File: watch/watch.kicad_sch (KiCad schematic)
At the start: 126 parts, among them IC1 MAX77659AENV+, IC2 MAX86141ENP+T, IC3 MAX32664GTGC+T, IC4 TXS0108ERGYR, IC6 MAX31341CETB+T, J1 TYPE-C-31-M-12, J2 Conn_01x01_Pin, J3 Conn_ARM_JTAG_SWD_10, J4 505110-2291, J5 Conn_01x01_Pin, J6 Conn_01x01_Pin, J7 Conn_01x01_Pin, Q1 BSS138, U1 nRF52840, U2 ICM-20602, Y1 FA-128_32.0000MF10Z-AJ5, Y2 CM7V-T1A-32.768kHz-6pF-20PPM-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, Y3 CM7V-T1A-32.768kHz-6pF-20PPM-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

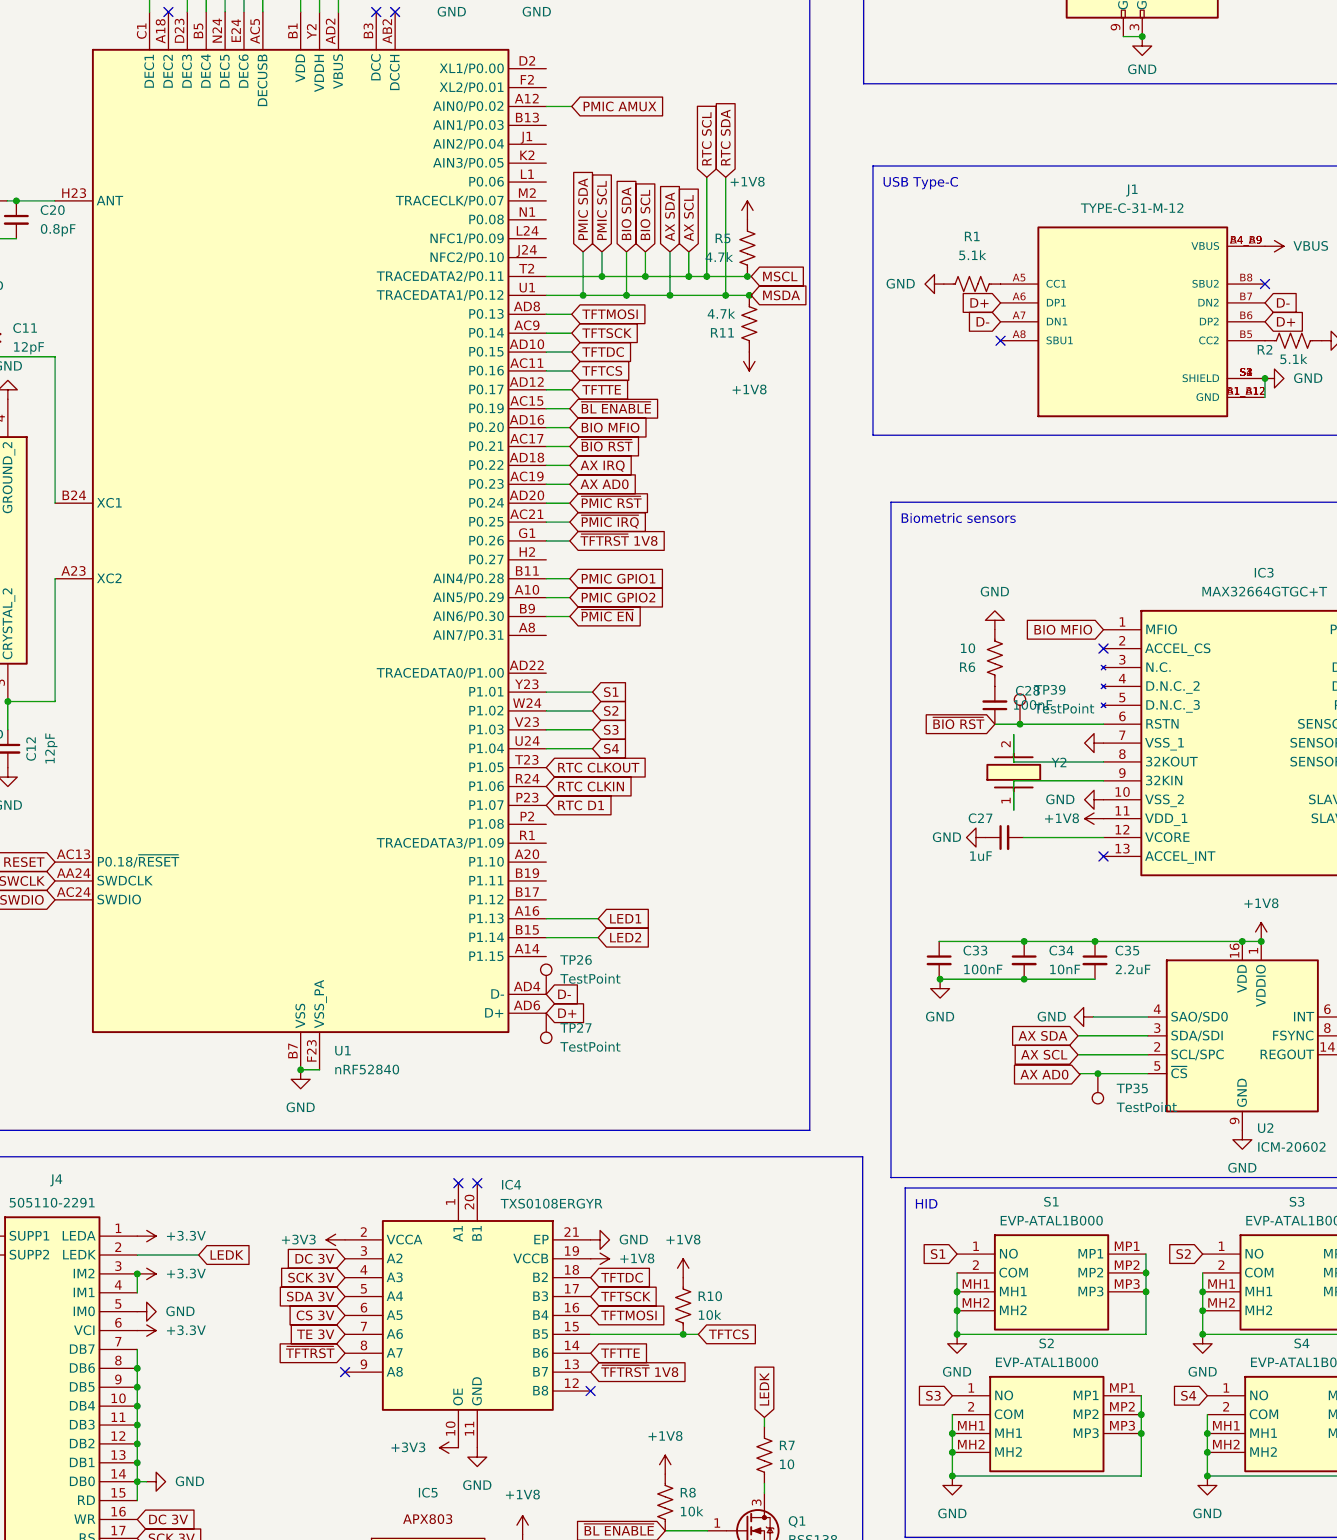
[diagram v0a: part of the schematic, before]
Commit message: rev1 done absolutely does not pass drc need to add ci
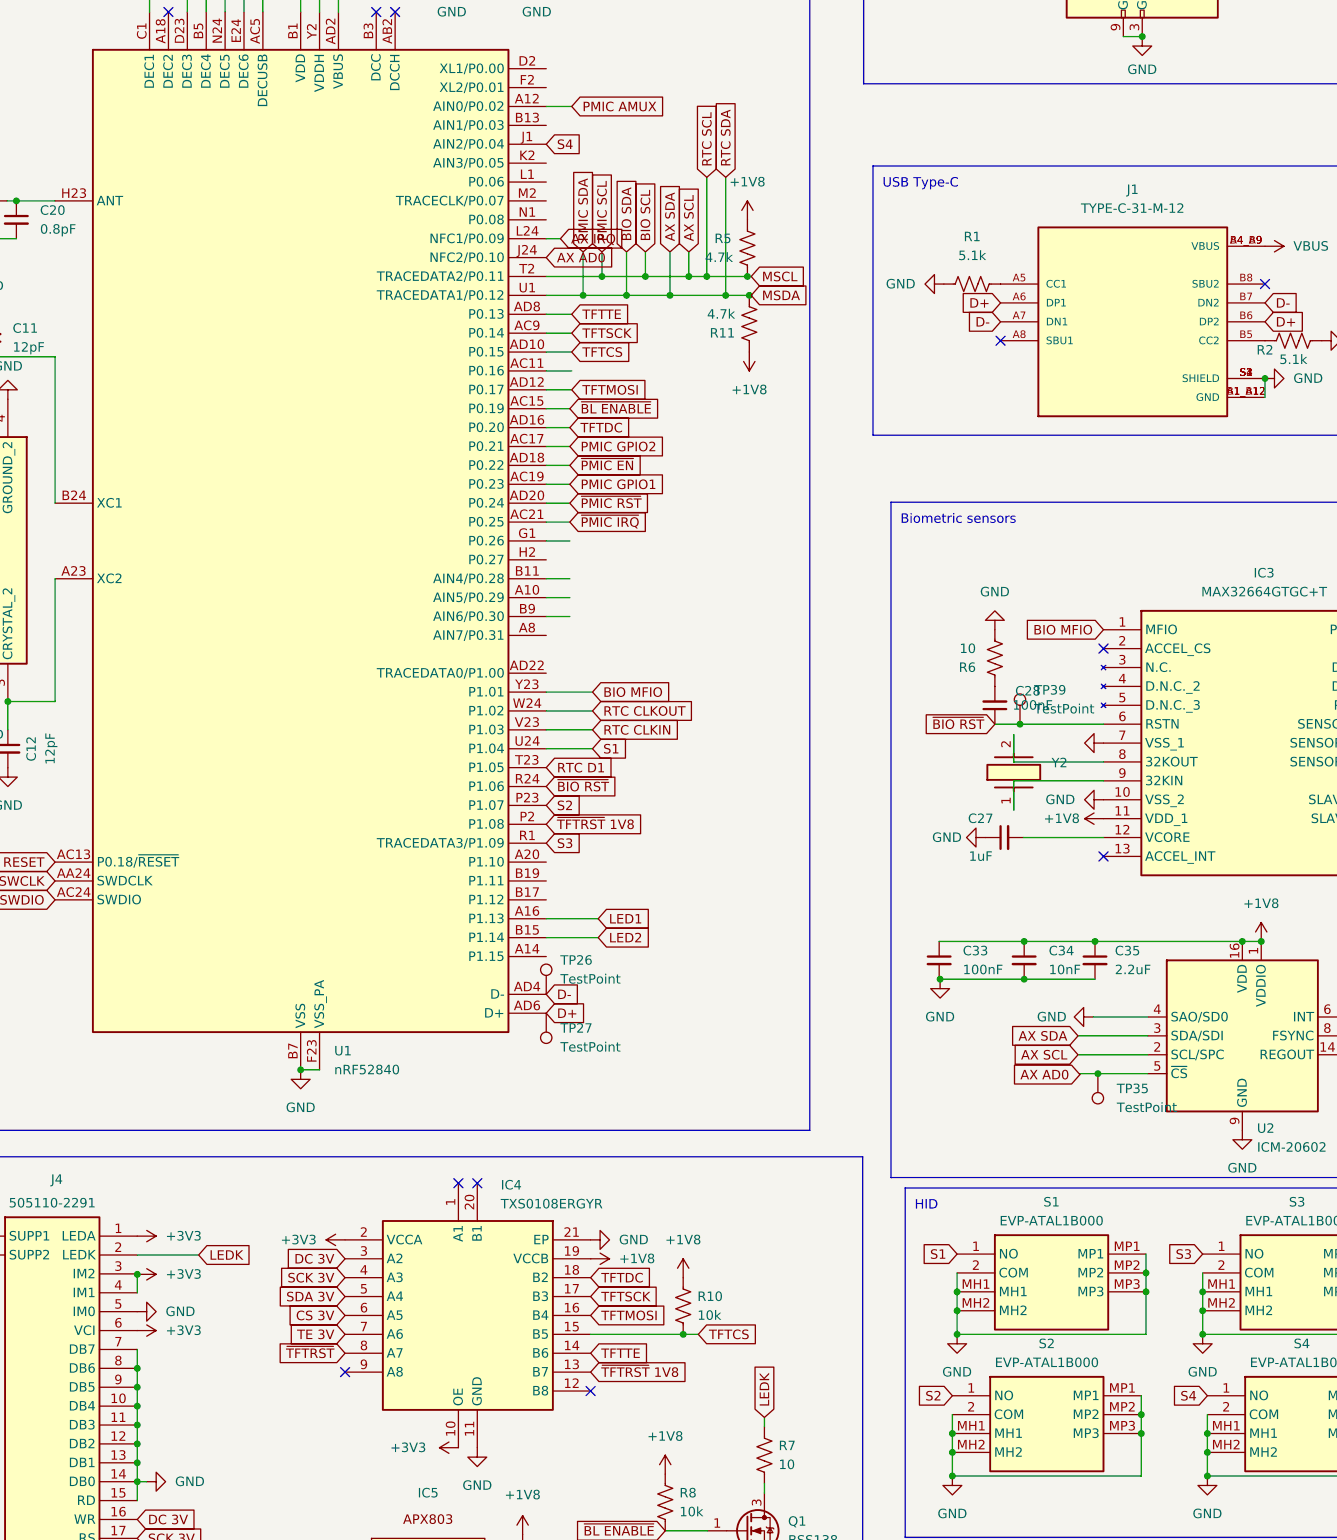
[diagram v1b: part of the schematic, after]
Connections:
- net +3.3V is gone; now on net +3V3: J4.1 (LEDA), J4.3 (IM2), J4.4 (IM1), J4.6 (VCI)
- net AX AD0: now also U1.J24 (NFC2/P0.10); no longer U1.AC19 (P0.23)
- net AX IRQ: now also U1.L24 (NFC1/P0.09); no longer U1.AD18 (P0.22)
- net BIO MFIO: now also U1.Y23 (P1.01); no longer U1.AD16 (P0.20)
- net PMIC GPIO1: now also U1.AC19 (P0.23); no longer U1.B11 (AIN4/P0.28)
- net PMIC GPIO2: now also U1.AC17 (P0.21); no longer U1.A10 (AIN5/P0.29)
- net RTC CLKIN: now also U1.V23 (P1.03); no longer U1.R24 (P1.06)
- net RTC CLKOUT: now also U1.W24 (P1.02); no longer U1.T23 (P1.05)
- net RTC D1: now also U1.T23 (P1.05); no longer U1.P23 (P1.07)
- net S1: now also U1.U24 (P1.04); no longer U1.Y23 (P1.01)
- net S2: now also S2.1 (NO), U1.P23 (P1.07); no longer S3.1 (NO), U1.W24 (P1.02)
- net S3: now also S3.1 (NO), U1.R1 (TRACEDATA3/P1.09); no longer S2.1 (NO), U1.V23 (P1.03)
- net S4: now also U1.J1 (AIN2/P0.04); no longer U1.U24 (P1.04)
- net TFTCS: now also U1.AD10 (P0.15); no longer U1.AC11 (P0.16)
- net TFTDC: now also U1.AD16 (P0.20); no longer U1.AD10 (P0.15)
- net TFTMOSI: now also U1.AD12 (P0.17); no longer U1.AD8 (P0.13)
- net TFTTE: now also U1.AD8 (P0.13); no longer U1.AD12 (P0.17)
- net ~{BIO RST}: now also U1.R24 (P1.06); no longer U1.AC17 (P0.21)
- net ~{PMIC EN}: now also U1.AD18 (P0.22); no longer U1.B9 (AIN6/P0.30)
- net ~{TFTRST} 1V8: now also U1.P2 (P1.08); no longer U1.G1 (P0.26)

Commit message: rev0.1 done, passes drc and jlc checks
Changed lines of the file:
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@@
   (no_connect (at 307.34 140.208))
   (no_connect (at 302.26 86.36))
-  (wire (pts (xy 118.745 105.41) (xy 122.174 105.41))
-    (stroke (width 0) (type default))
-  )
   (wire (pts (xy 118.745 29.845) (xy 130.175 29.845))
     (stroke (width 0) (type default))
@@
     (stroke (width 0) (type default))
   )
-  (wire (pts (xy 118.745 128.27) (xy 121.92 128.27))
-    (stroke (width 0) (type default))
-  )
   (wire (pts (xy 392.43 84.455) (xy 392.43 85.09))
     (stroke (width 0) (type default))
@@
     (stroke (width 0) (type default))
   )
-  (wire (pts (xy 118.745 138.43) (xy 121.92 138.43))
-    (stroke (width 0) (type default))
-  )
   (wire (pts (xy 118.745 120.65) (xy 121.92 120.65))
     (stroke (width 0) (type default))
@@
     (stroke (width 0) (type default))
   )
-  (wire (pts (xy 118.745 133.35) (xy 121.92 133.35))
-    (stroke (width 0) (type default))
-  )
   (wire (pts (xy 146.05 95.25) (xy 146.304 95.25))
     (stroke (width 0) (type default))
@@
     (stroke (width 0) (type default))
   )
-  (wire (pts (xy 118.745 135.89) (xy 121.92 135.89))
-    (stroke (width 0) (type default))
-  )

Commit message: change mounting clearances, add expansion connector
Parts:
- removed TP10, TP11, TP12, TP13, TP14, TP16, TP17, TP18, TP19, TP20, TP21, TP22, TP23, TP24, TP25, TP26, TP27, TP28, TP29, TP3, TP30, TP31, TP32, TP33, TP34, TP35, TP36, TP37, TP38, TP39, TP4, TP5, TP6, TP7, TP8, TP9: TestPoint, TestPoint:TestPoint_Pad_D1.0mm, symbol Connector:TestPoint
- added J8: Conn_01x04_Pin, Connector_PinHeader_2.54mm:PinHeader_1x04_P2.54mm_Vertical, symbol Connector:Conn_01x04_Pin
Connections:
- net +3V3: now also J8.4 (Pin_4)
- net -BATT: now also J8.1 (Pin_1)
- net AX SCL: now also J8.2 (Pin_2)
- net AX SDA: now also J8.3 (Pin_3)
